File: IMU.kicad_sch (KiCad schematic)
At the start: 8 parts, among them U3 LSM6DSOXTR

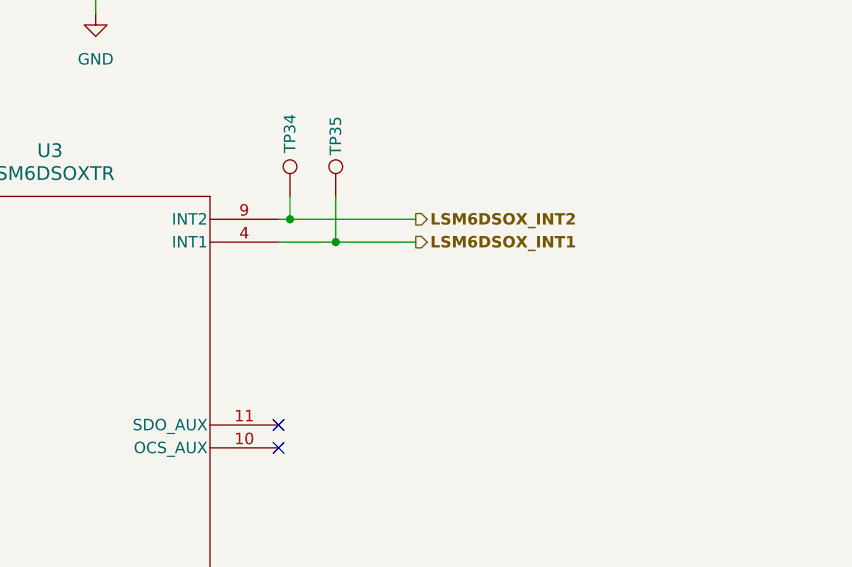
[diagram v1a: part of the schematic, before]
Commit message: Added comment regarding push-pull default for INT1 and INT2
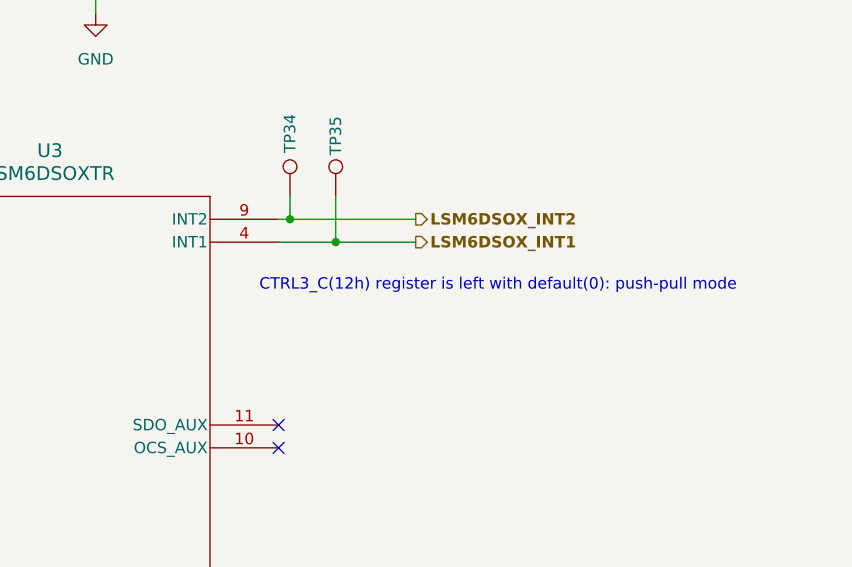
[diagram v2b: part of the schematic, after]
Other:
- note added: "CTRL3_C(12h) register is left with default(0): push-pull mode"
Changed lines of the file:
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@@
+		)
+	)
+	(text "CTRL3_C(12h) register is left with default(0): push-pull mode"
+		(exclude_from_sim yes)
+		(at 190.754 68.326 0)
+		(effects
+			(font
+				(size 1.27 1.27)
+			)
 		)
 	)
@@
 			"Fxf/FxcX/xcXF/8XFxf/FxcX/yAgIP8vLy//FxcX/xcXF/8XFxf/FxcX/xcXF/8XFxf/FxcX/xcX"
 			"F/8XFxf/FxcX/xcXF/8aGhr/NDQ0/xcXF/8XFxf/FxcX/xcXF/8XFxf/FxcX/xcXF/8XFxf/FxcX"
-			"/xcXF/8XFxf/FxcX/xcXF/8XFxf/FxcX/xcXF/8XFxf/FxcX/xcXF/8XFw=="
-		)
-	)
+			"/xcXF/8XFxf/FxcX/xcXF/8XFxf/FxcX/xcXF/8XFxf/FxcX/xcXF/8XF4jrx38AAICNiOvHfwAA"
+			"YJeI68d/AACgwIjrx38AABDSiOvHfwAAYESG68d/AACQlobrx38AABidhuvHfwAA0H6R68d/AADA"
+			"kpHrx38AAHiXkevHfwAAIgQAABoAAAC4mpHrx38AAOMNAABNVNWqAAAAAAAAAAABAAAAAAAAAHBF"
+			"sB4BAAAA6HuI68d/AAC4mpHrx38AAAAAAAAAAAAAAAAAAAAAAAAAAAAAAAAAALQBAAAAAAAA7AEA"
+			"ABUAAAABAAAAAAAAAECbkevHfwAAGAAAAMd/AABwRrAeAQAAAAEAAADHfwAASwQAAE1U1aruAQAA"
+			"BAAAAO4BAAAKAAAAGAAAAMd/AABw2cgOAQAAAAEAAADHfwAAfgYAAGg2+Z7uAQAACwAAAO4BAAAR"
+			"AAAAcNnIDgEAAAAAAAAAAAAAAAAAAAAAAAAA7gEAAAsAAADuAQAAEQAAABgAAAAAYAAAsCfODgEA"
+			"AAABAAAAaDf5mDCbkevHfwAA7gEAABMAAADuAQAAGAAAALAnzg4BAAAAAAAAAAAAAAAAAAAAAAAA"
+			"AO4BAAATAAAA7gEAABgAAAAYAAAAx38AAPATpw4BAAAAAQAAAAAAAADAkhwCAGAAAO4BAAAaAAAA"
+			"7gEAACEAAADwE6cOAQAAAAAAAAAAAAAAAAAAAAAAAADuAQAAGgAAAO4BAAAhAAAAGAAAAMd/AACw"
+			"RbAeAQAAAAEAAADHfwAAcwQAAABgAADuAQAAIwAAAO4BAAApAAAAsEWwHgEAAAAAAAAAAAAAAAAA"
+			"AAAAAAAA7gEAACMAAADuAQAAKQAAABgAAABNVNWqsEawHgEAAAABAAAAAGAAAAidkevHfwAA7gEA"
+			"ACsAAADuAQAAMAAAALBGsB4BAAAAAAAAAAAAAAAAAAAAAAAAAO4BAAArAAAA7gEAADAAAAAYAAAA"
+			"x38AALBGsB4BAAAAAQAAAAAAAAB/BgAAAGAAAO4BAAArAAAA7gEAADAAAACwRrAeAQAAAAAAAAAA"
+			"AAAAAAAAAAAAAADuAQAAKwAAAO4BAAAwAAAABAAAAAAAAAD4m5Hrx38AAFCckevHfwAAqJyR68d/"
+			"AAAAnZHrx38AAMMEAADHfwAA2J2R68d/AADuDQAAAAAAAAAAAAAAAAAAGAAAAMd/AABw2cgOAQAA"
+			"AAEAAAAAAAAAfwYAAH9FharuAQAACwAAAO4BAAARAAAAcNnIDgEAAAAAAAAAAAAAAAAAAAAAAAAA"
+			"7gEAAAsAAADuAQAAEQAAABgAAAD4fwAAsCfODgEAAAABAAAAAGAAAAAAAAAAAAAA7gEAABMAAADu"
+			"AQAAGAAAALAnzg4BAAAAAAAAAAAAAAAAAAAAAAAAAO4BAAATAAAA7gEAAA=="
+		)
+	)
